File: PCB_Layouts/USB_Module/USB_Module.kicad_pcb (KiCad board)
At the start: 2 copper layers, 33.5 x 25.2 mm, 4 parts, among them J1 USB_A, J2 Conn_01x10_Socket, J3 Conn_01x10_Socket

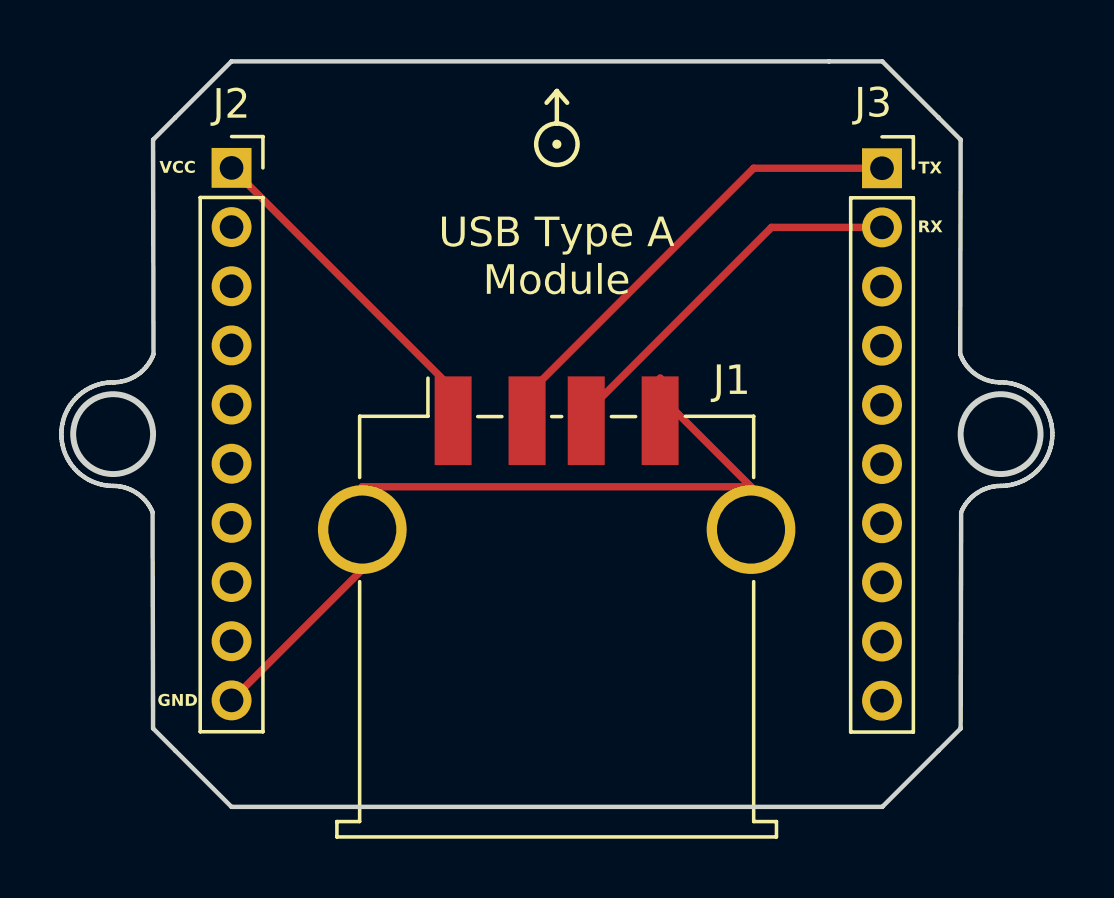
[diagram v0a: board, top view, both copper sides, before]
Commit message: Updating the USB module to adapt to the quote
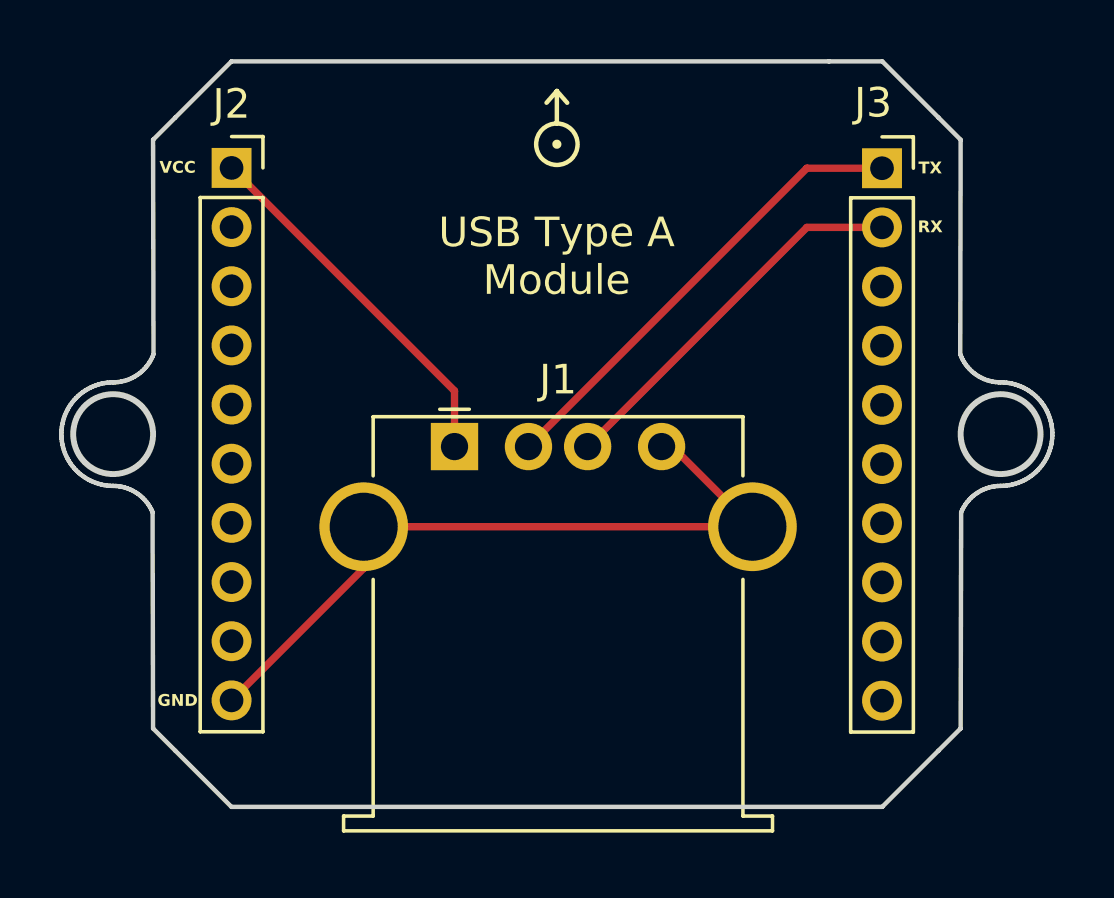
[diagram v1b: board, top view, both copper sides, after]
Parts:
- J1: footprint Connector_USB:USB_A_TE_292303-7_Horizontal -> Connector_USB:USB_A_Stewart_SS-52100-001_Horizontal
- moved J1 6.50 mm to (140.9, 97.1)
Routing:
- net Net-(J1-GND): track 27.1 -> 25.1 mm
- net Net-(J1-VBUS): track 11.0 -> 12.9 mm
